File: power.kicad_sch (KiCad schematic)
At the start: 25 parts, among them J1 XT30PW-M, U1 TPS562201DDCR, U2 TPS562201DDCR, U3 DMG3415U-7

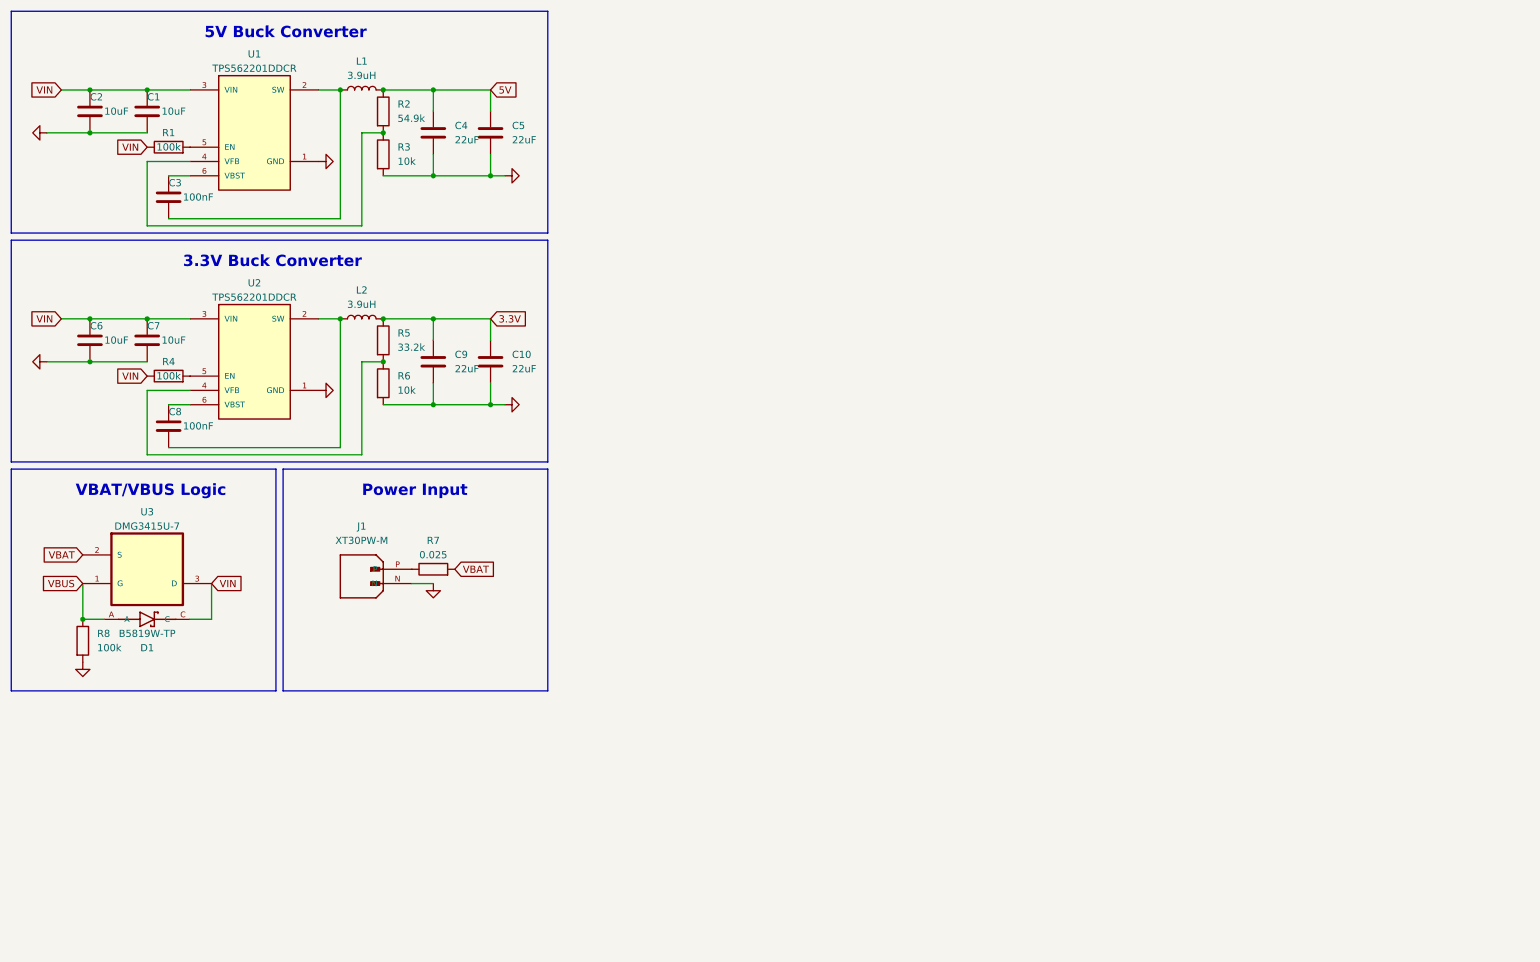
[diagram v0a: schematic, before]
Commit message: Organized Schematics & Fixed Notes
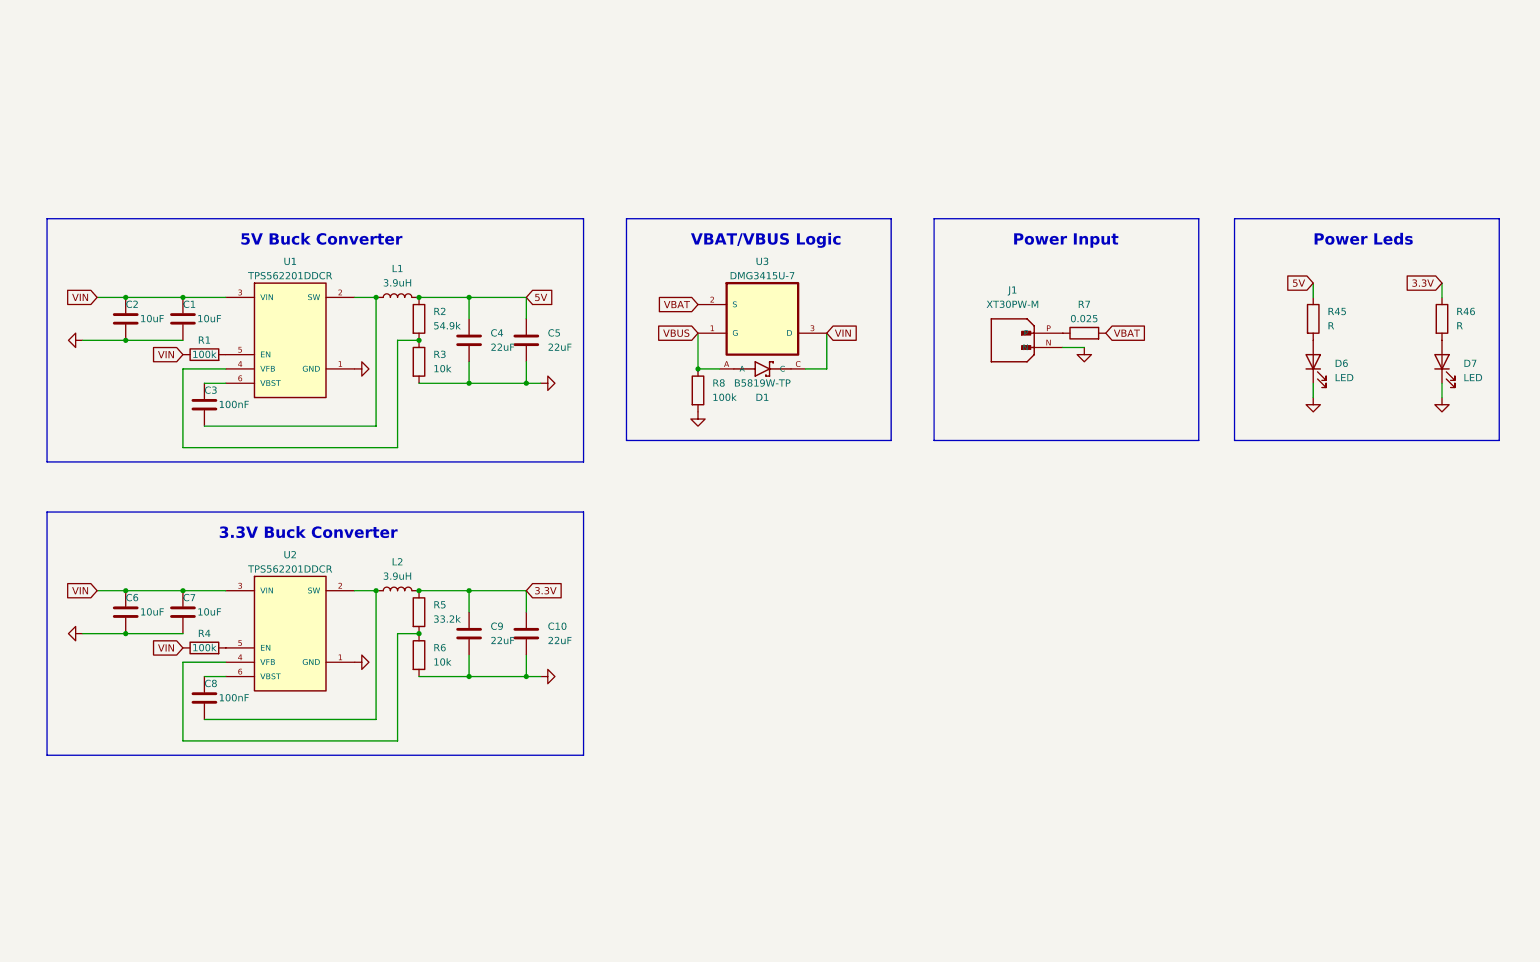
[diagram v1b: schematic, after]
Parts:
- added D6, D7: LED, symbol Device:LED
- added R45, R46: R, symbol Device:R
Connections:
- net 3.3V: now also R46.1
- net 5V: now also R45.1
- net GND: now also D6.1 (K), D7.1 (K)
- new net: D6.2 (A), R45.2
- new net: D7.2 (A), R46.2
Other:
- note added: "Power Leds"
- company: (none) -> nyuad.space
- title: (none) -> Power Schematics
- moved on the sheet: C1, C10, C2, C3, C4, C5, C6, C7, C8, C9, D1, J1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

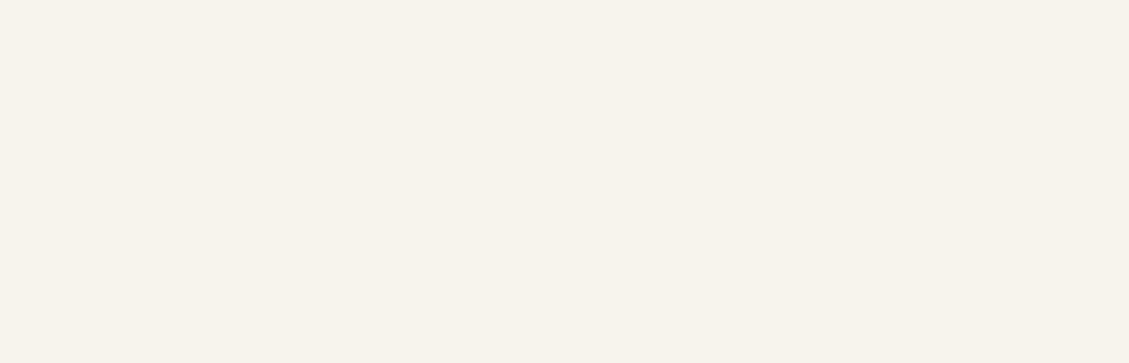
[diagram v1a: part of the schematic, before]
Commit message: Added OSH Logo
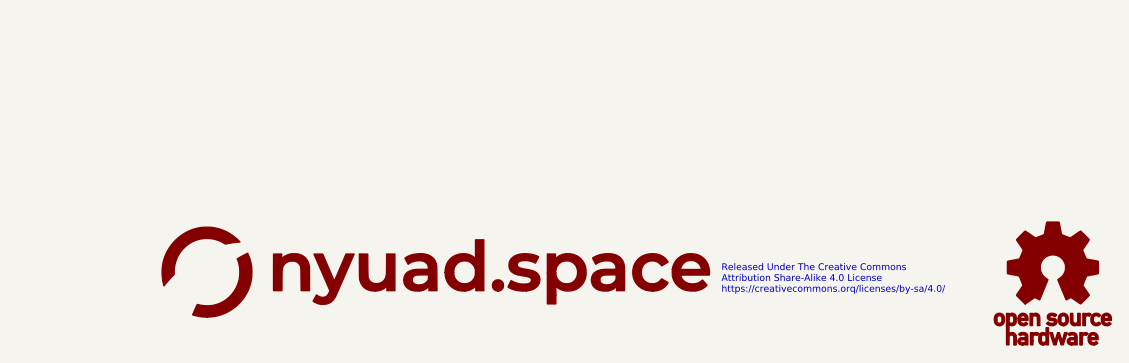
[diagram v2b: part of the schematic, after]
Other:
- note added: "Released Under The Creative Commons Attribution Share-Alike 4.0 License https://creativecommons.orq/licenses/by-sa/4.0/"
- company: nyuad.space -> Aether Flight Computer
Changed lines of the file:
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@@
   (title_block
     (title "Power Schematics")
-    (company "nyuad.space")
-    (comment 1 "Aether Flight Computer")
+    (company "Aether Flight Computer")
   )
   (junction (at 34.29 72.39) (diameter 0) (color 0 0 0 0)
@@
   (text "VBAT/VBUS Logic" (at 134.62 55.88 0)
     (effects (font (size 2 2) (thickness 0.8) bold) (justify left bottom))
+  )
+  (text "Released Under The Creative Commons\nAttribution Share-Alike 4.0 License\nhttps://creativecommons.orq/licenses/by-sa/4.0/"
+    (at 240.03 175.26 0)
+    (effects (font (face "KiCad Font") (size 0.75 0.75)) (justify left bottom))
   )
   (text "Power Input" (at 191.77 55.88 0)
@@
     )
   )
+  (symbol (lib_id "osh_logo:LOGO") (at 276.86 173.99 0) (unit 1)
+    (in_bom yes) (on_board yes) (dnp no) (fields_autoplaced)
+    (property "Reference" "#G1" (at 276.86 167.7874 0)
+      (effects (font (size 1.27 1.27)) hide)
+    )
+    (property "Value" "LOGO" (at 276.86 180.1926 0)
+      (effects (font (size 1.27 1.27)) hide)
+    )
+    (property "Footprint" "" (at 276.86 173.99 0)
+      (effects (font (size 1.27 1.27)) hide)
+    )
+    (property "Datasheet" "" (at 276.86 173.99 0)
+      (effects (font (size 1.27 1.27)) hide)
+    )
+    (instances
+      (project "aether"
+        (path "/e12346fa-509d-4de9-8ab1-dced307292db"
+          (reference "#G1") (unit 1)
+        )
+        (path "/e12346fa-509d-4de9-8ab1-dced307292db/c23bfb85-0f05-40d7-b8da-b36b200d10d9"
+          (reference "#G10") (unit 1)
+        )
+      )
+    )
+  )
   (symbol (lib_id "Device:R") (at 48.26 127 90) (unit 1)
     (in_bom yes) (on_board yes) (dnp no)
@@
         )
       )
+    )
+  )
+  (symbol (lib_id "nyuad_space:LOGO") (at 208.28 172.72 0) (unit 1)
+    (in_bom yes) (on_board yes) (dnp no) (fields_autoplaced)
+    (property "Reference" "#G2" (at 208.28 168.3609 0)
+      (effects (font (size 1.27 1.27)) hide)
+    )
+    (property "Value" "LOGO" (at 208.28 177.0791 0)
+      (effects (font (size 1.27 1.27)) hide)
+    )
+    (property "Footprint" "" (at 208.28 172.72 0)
+      (effects (font (size 1.27 1.27)) hide)
+    )
+    (property "Datasheet" "" (at 208.28 172.72 0)
+      (effects (font (size 1.27 1.27)) hide)
+    )
+    (instances
+      (project "aether"
+        (path "/e12346fa-509d-4de9-8ab1-dced307292db"
+          (reference "#G2") (unit 1)
+        )
+        (path "/e12346fa-509d-4de9-8ab1-dced307292db/c23bfb85-0f05-40d7-b8da-b36b200d10d9"
+          (reference "#G9") (unit 1)
+        )
+      )

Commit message: Updated files
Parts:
- removed U3: DMG3415U-7, SOT95P240X105-3N, symbol DMG3415U-7:DMG3415U-7
- added Q8: PNP, symbol Simulation_SPICE:PNP
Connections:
- net VBAT: now also Q8.1 (C)
- net VBUS: now also Q8.2 (B)
- net VIN: now also Q8.3 (E)
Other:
- note removed: "Released Under The Creative Commons Attribution Share-Alike 4.0 License https://creativecommons.orq/licenses/by-sa/4.0/"
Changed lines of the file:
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@@
+    (stroke (width 0) (type default))
+  )
+  (wire (pts (xy 135.89 66.04) (xy 139.7 66.04))
     (stroke (width 0) (type default))
   )
@@
     (stroke (width 0) (type default))
   )
-  (wire (pts (xy 135.89 71.12) (xy 135.89 77.47))
+  (wire (pts (xy 135.89 66.04) (xy 135.89 77.47))
     (stroke (width 0) (type default))
   )
@@
     (stroke (width 0) (type default))
   )
+  (wire (pts (xy 147.32 71.12) (xy 158.75 71.12))
+    (stroke (width 0) (type default))
+  )
   (wire (pts (xy 44.45 77.47) (xy 44.45 91.44))
     (stroke (width 0) (type default))
@@
   )
   (wire (pts (xy 95.25 116.84) (xy 105.41 116.84))
+    (stroke (width 0) (type default))
+  )
+  (wire (pts (xy 135.89 60.96) (xy 147.32 60.96))
     (stroke (width 0) (type default))
   )
@@
   (text "VBAT/VBUS Logic" (at 134.62 55.88 0)
     (effects (font (size 2 2) (thickness 0.8) bold) (justify left bottom))
-  )
-  (text "Released Under The Creative Commons\nAttribution Share-Alike 4.0 License\nhttps://creativecommons.orq/licenses/by-sa/4.0/"
-    (at 240.03 175.26 0)
-    (effects (font (face "KiCad Font") (size 0.75 0.75)) (justify left bottom))
   )
   (text "Power Input" (at 191.77 55.88 0)
@@
     )
   )
-  (global_label "VBAT" (shape input) (at 135.89 66.04 180) (fields_autoplaced)
+  (global_label "VBAT" (shape input) (at 135.89 60.96 180) (fields_autoplaced)
     (effects (font (size 1.27 1.27)) (justify right))
-    (property "Intersheetrefs" "${INTERSHEET_REFS}" (at 128.49 66.04 0)
-      (effects (font (size 1.27 1.27)) (justify right) hide)
-    )
-  )
-  (global_label "VBUS" (shape input) (at 135.89 71.12 180) (fields_autoplaced)
+    (property "Intersheetrefs" "${INTERSHEET_REFS}" (at 128.49 60.96 0)
+      (effects (font (size 1.27 1.27)) (justify right) hide)
+    )
+  )
+  (global_label "VBUS" (shape input) (at 135.89 66.04 180) (fields_autoplaced)
     (effects (font (size 1.27 1.27)) (justify right))
-    (property "Intersheetrefs" "${INTERSHEET_REFS}" (at 128.0062 71.12 0)
+    (property "Intersheetrefs" "${INTERSHEET_REFS}" (at 128.0062 66.04 0)
       (effects (font (size 1.27 1.27)) (justify right) hide)
     )
@@
     )
   )
+  (symbol (lib_id "Simulation_SPICE:PNP") (at 144.78 66.04 0) (unit 1)
+    (in_bom yes) (on_board yes) (dnp no) (fields_autoplaced)
+    (property "Reference" "Q8" (at 149.86 64.77 0)
+      (effects (font (size 1.27 1.27)) (justify left))
+    )
+    (property "Value" "PNP" (at 149.86 67.31 0)
+      (effects (font (size 1.27 1.27)) (justify left))
+    )
+    (property "Footprint" "" (at 180.34 66.04 0)
+      (effects (font (size 1.27 1.27)) hide)
+    )
+    (property "Datasheet" "~" (at 180.34 66.04 0)
+      (effects (font (size 1.27 1.27)) hide)
+    )
+    (property "Sim.Device" "PNP" (at 144.78 66.04 0)
+      (effects (font (size 1.27 1.27)) hide)
+    )
+    (property "Sim.Type" "GUMMELPOON" (at 144.78 66.04 0)
+      (effects (font (size 1.27 1.27)) hide)
+    )
+    (property "Sim.Pins" "1=C 2=B 3=E" (at 144.78 66.04 0)
+      (effects (font (size 1.27 1.27)) hide)
+    )
+    (pin "1")
+    (pin "2")
+    (pin "3")
+    (instances
+      (project "aether"
+        (path "/e12346fa-509d-4de9-8ab1-dced307292db/c23bfb85-0f05-40d7-b8da-b36b200d10d9"
+          (reference "Q8") (unit 1)
+        )
+      )
+    )
+  )
   (symbol (lib_id "power:GND") (at 26.67 72.39 270) (unit 1)
     (in_bom yes) (on_board yes) (dnp no) (fields_autoplaced)
@@
         )
       )
-    )
-  )
-  (symbol (lib_id "DMG3415U-7:DMG3415U-7") (at 147.32 68.58 0) (unit 1)
-    (in_bom yes) (on_board yes) (dnp no)
-    (property "Reference" "U3" (at 147.32 58.42 0)
-      (effects (font (size 1.27 1.27)))
-    )
-    (property "Value" "DMG3415U-7" (at 147.32 60.96 0)
-      (effects (font (size 1.27 1.27)))
-    )
-    (property "Footprint" "SOT95P240X105-3N" (at 147.32 68.58 0)
-      (effects (font (size 1.27 1.27)) (justify bottom) hide)
-    )
-    (property "Datasheet" "" (at 147.32 68.58 0)
-      (effects (font (size 1.27 1.27)) hide)
-    )
-    (property "MPN" "DMG3415U-7" (at 147.32 68.58 0)
-      (effects (font (size 1.27 1.27)) (justify bottom) hide)
-    )
-    (property "OC_FARNELL" "1843688" (at 147.32 68.58 0)
-      (effects (font (size 1.27 1.27)) (justify bottom) hide)
-    )
-    (property "OC_NEWARK" "12T2026" (at 147.32 68.58 0)
-      (effects (font (size 1.27 1.27)) (justify bottom) hide)
-    )
-    (property "SUPPLIER" "Diodes Inc" (at 147.32 68.58 0)
-      (effects (font (size 1.27 1.27)) (justify bottom) hide)
-    )
-    (property "PACKAGE" "SOT-23-3" (at 147.32 68.58 0)
-      (effects (font (size 1.27 1.27)) (justify bottom) hide)
-    )
-    (pin "1")
-    (pin "2")
-    (pin "3")
-    (instances
-      (project "aether"
-        (path "/e12346fa-509d-4de9-8ab1-dced307292db"
-          (reference "U3") (unit 1)
-        )
-        (path "/e12346fa-509d-4de9-8ab1-dced307292db/c23bfb85-0f05-40d7-b8da-b36b200d10d9"
-          (reference "U1") (unit 1)
-        )
-      )
